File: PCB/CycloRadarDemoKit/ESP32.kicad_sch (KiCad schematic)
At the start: 18 parts, among them SW101 RESET, SW102 BOOT MODE, U101 ESP32-WROVER-E-N16R8

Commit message: PCB, 3Dmodel
mockup PCB version done, schcematic exported to latex, 3D model generated and exported to latex
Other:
- title: Safety Ride Radar Sensor -> Radar Safety Sensor
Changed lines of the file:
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@@
   (paper "A4")
   (title_block
-    (title "Safety Ride Radar Sensor")
-    (date "2023-12-19")
-    (rev "Rev.: WIP")
+    (title "Radar Safety Sensor")
+    (date "2023-12-20")
+    (rev "Rev.: 1")
     (company "ALPS Electric Czech, s.r.o.")
     (comment 1 "Designed by Martin Tavoda")

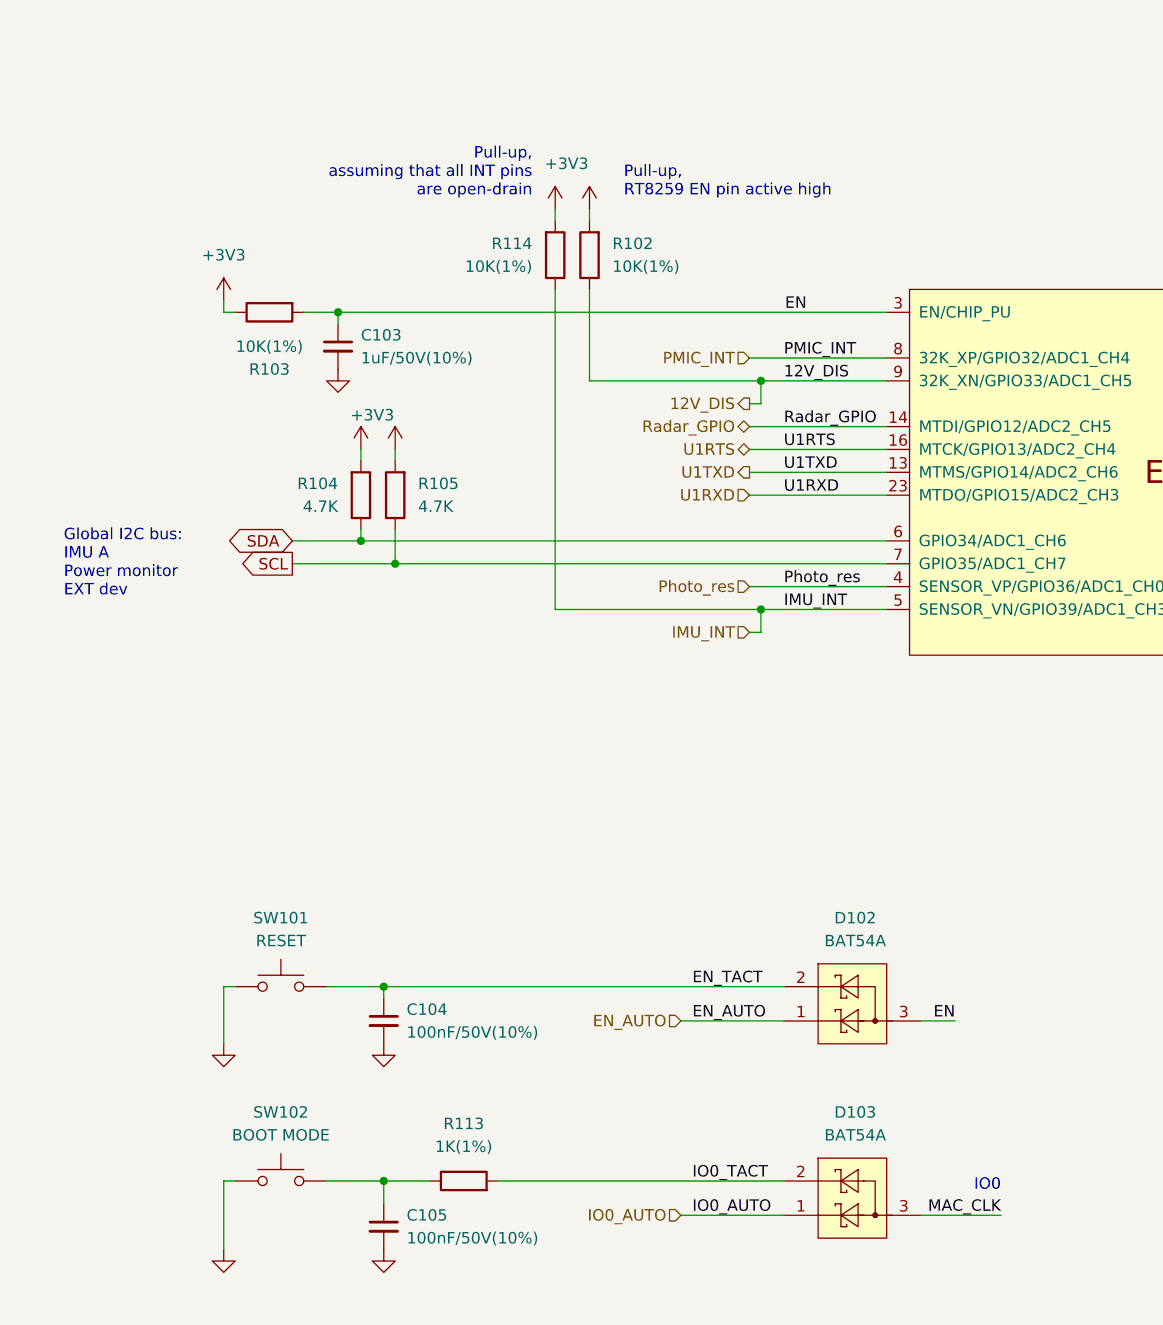
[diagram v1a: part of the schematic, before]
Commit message: sortingAbbr, cosmetics schematic, export schematic to thesis
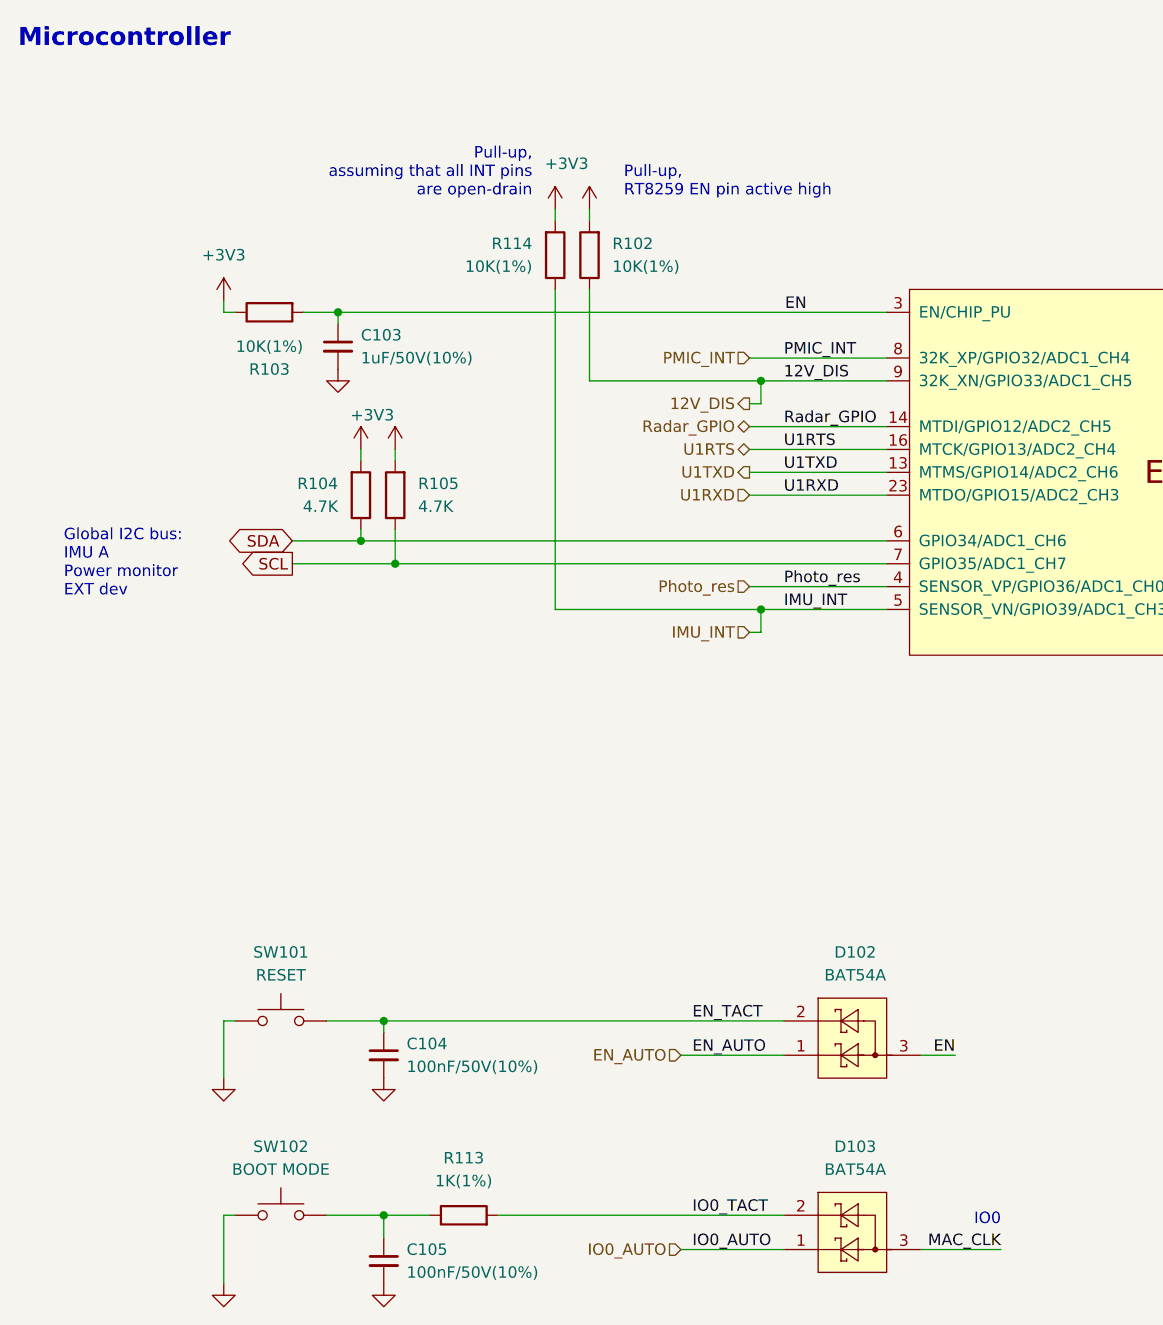
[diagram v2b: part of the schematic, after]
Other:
- note added: "Microcontroller"
- moved on the sheet: C104, C105, D102, D103, R113, SW101, SW102

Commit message: PCB small updates, schemtatic cosmetics, SEP FINAL
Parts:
- C101: footprint (none) -> Capacitor_SMD:C_0603_1608Metric; LCSC (none) -> C19702
- C102: LCSC (none) -> C19702
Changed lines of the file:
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@@
       (effects (font (size 1.27 1.27)) (justify left))
     )
-    (property "Footprint" "" (at 189.23 44.45 0)
+    (property "Footprint" "Capacitor_SMD:C_0603_1608Metric" (at 189.23 44.45 0)
       (effects (font (size 1.27 1.27)) hide)
     )
     (property "Datasheet" "~" (at 189.23 44.45 0)
+      (effects (font (size 1.27 1.27)) hide)
+    )
+    (property "LCSC" "C19702" (at 189.23 44.45 0)
       (effects (font (size 1.27 1.27)) hide)
     )
@@
       (effects (font (size 1.27 1.27)) hide)
     )
-    (property "LCSC" "" (at 184.15 44.45 0)
+    (property "LCSC" "C19702" (at 184.15 44.45 0)
       (effects (font (size 1.27 1.27)) hide)
     )

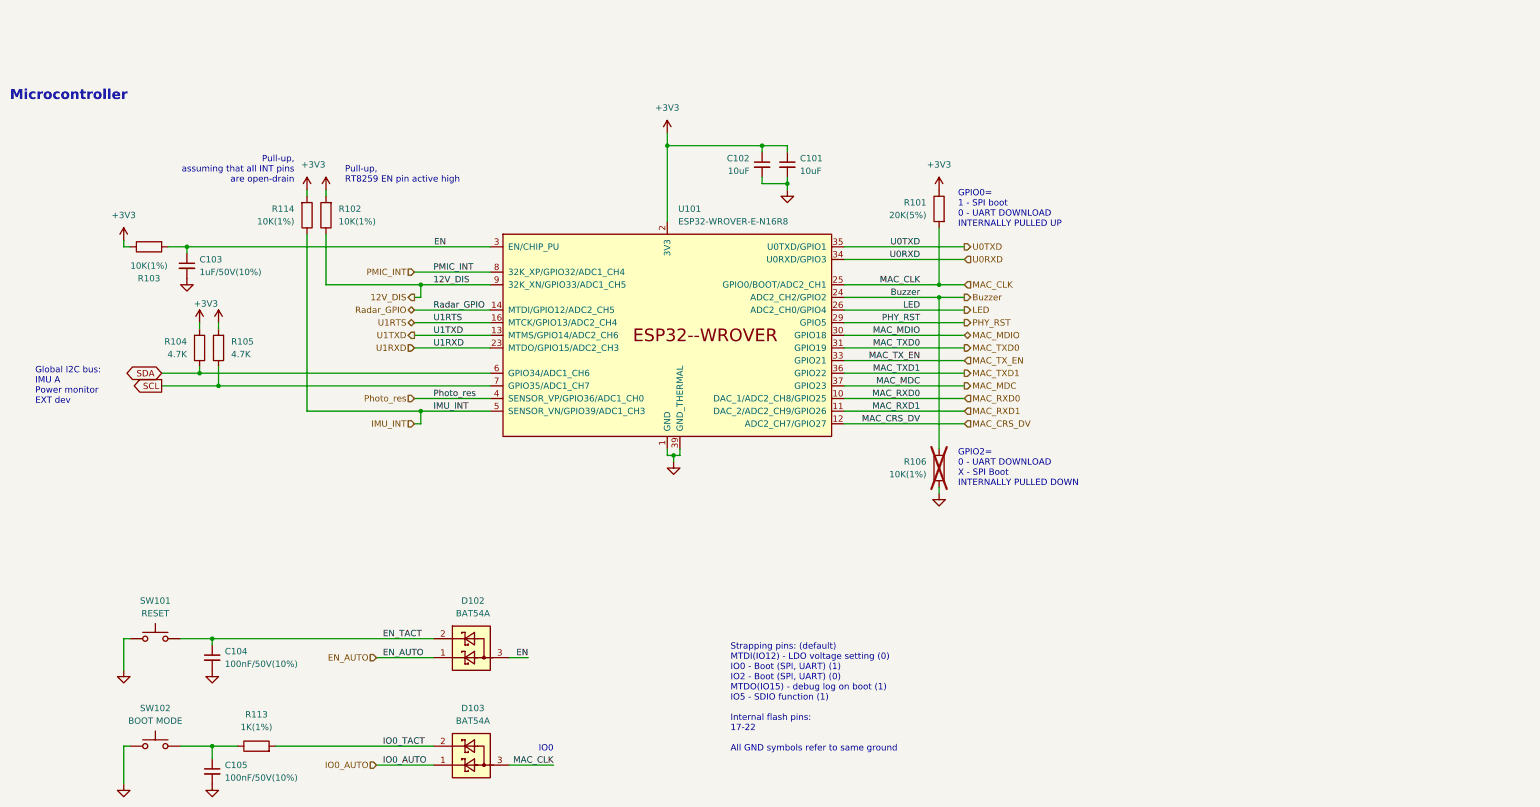
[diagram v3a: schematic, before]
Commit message: All peripherals checked, changed ESP32 pinout
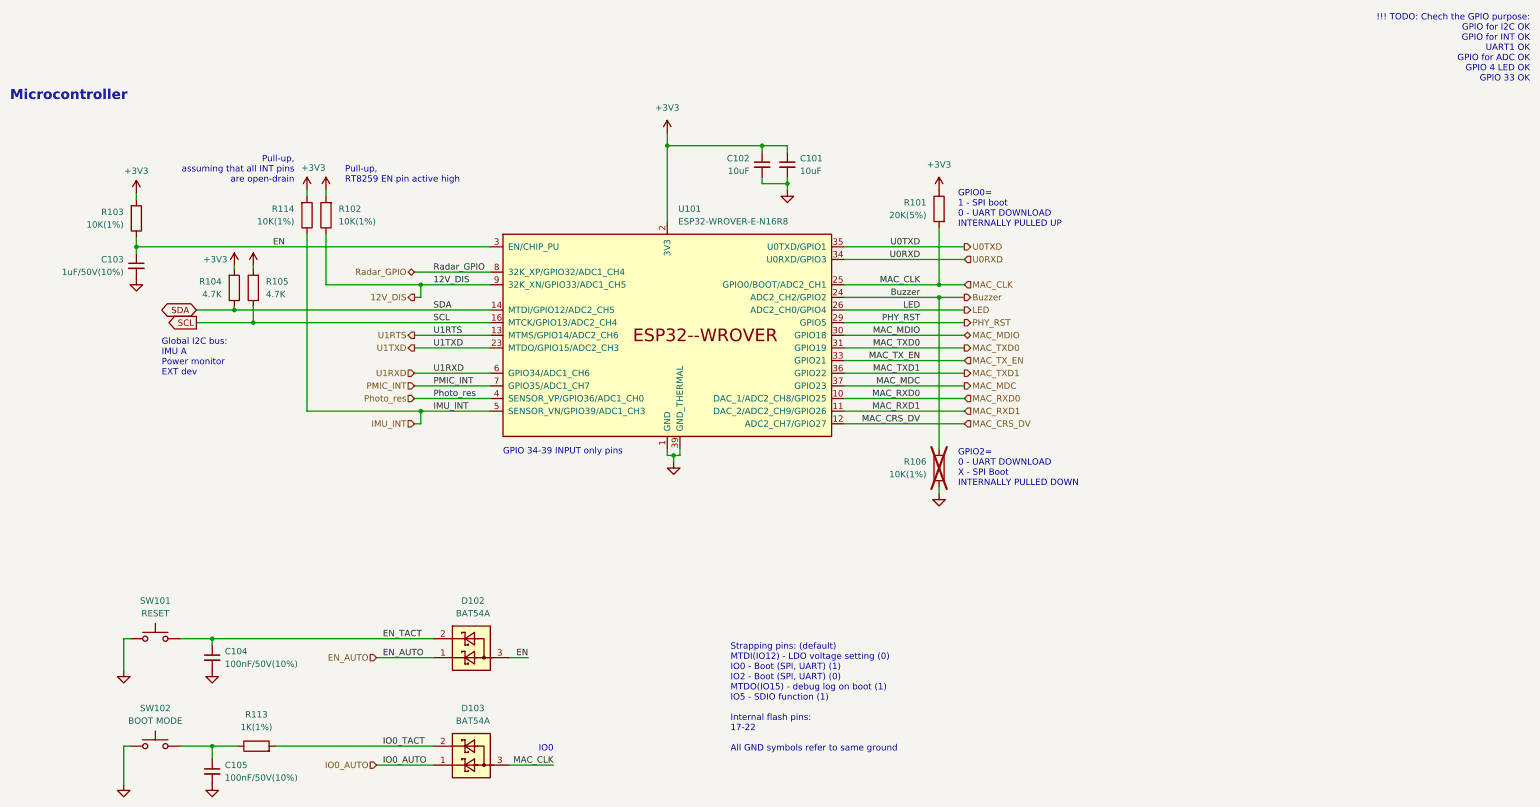
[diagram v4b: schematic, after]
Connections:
- net +3V3: now also R103.2; no longer R103.1
- net EN: now also R103.1; no longer R103.2
- net PMIC_INT: now also U101.7 (GPIO35/ADC1_CH7); no longer U101.8 (32K_XP/GPIO32/ADC1_CH4)
- net Radar_GPIO: now also U101.8 (32K_XP/GPIO32/ADC1_CH4); no longer U101.14 (MTDI/GPIO12/ADC2_CH5)
- net SCL: now also U101.16 (MTCK/GPIO13/ADC2_CH4); no longer U101.7 (GPIO35/ADC1_CH7)
- net SDA: now also U101.14 (MTDI/GPIO12/ADC2_CH5); no longer U101.6 (GPIO34/ADC1_CH6)
- net U1RTS: now also U101.13 (MTMS/GPIO14/ADC2_CH6); no longer U101.16 (MTCK/GPIO13/ADC2_CH4)
- net U1RXD: now also U101.6 (GPIO34/ADC1_CH6); no longer U101.23 (MTDO/GPIO15/ADC2_CH3)
- net U1TXD: now also U101.23 (MTDO/GPIO15/ADC2_CH3); no longer U101.13 (MTMS/GPIO14/ADC2_CH6)
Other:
- note added: "!!! TODO: Chech the GPIO purpose: GPIO for I2C OK GPIO for INT OK UART1 OK GPIO for ADC OK GPIO 4 LED OK GPIO 33 OK"
- note added: "GPIO 34-39 INPUT only pins"
- moved on the sheet: C103, R103, R104, R105

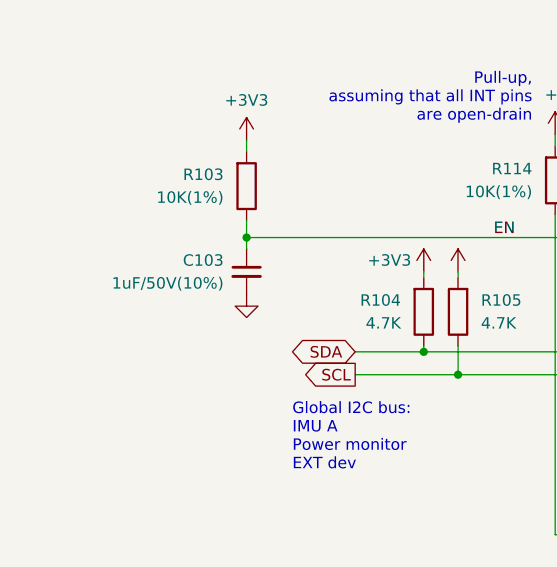
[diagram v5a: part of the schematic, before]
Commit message: Parts ordered on PCB, 1206->0803 10uF, 0803->0402 1uF
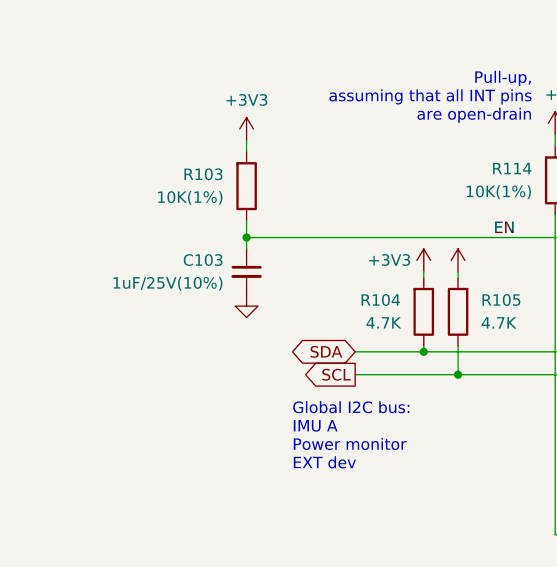
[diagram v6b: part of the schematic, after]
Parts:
- C103: value 1uF/50V(10%) -> 1uF/25V(10%); footprint Capacitor_SMD:C_0603_1608Metric -> Capacitor_SMD:C_0402_1005Metric; LCSC C15849 -> C52923
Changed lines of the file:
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@@
       (effects (font (size 1.27 1.27)) (justify left))
     )
-    (property "Value" "1uF/50V(10%)" (at 55.88 66.0463 0)
+    (property "Value" "1uF/25V(10%)" (at 55.88 66.0463 0)
       (effects (font (size 1.27 1.27)) (justify left))
     )
-    (property "Footprint" "Capacitor_SMD:C_0603_1608Metric" (at 58.42 64.77 0)
+    (property "Footprint" "Capacitor_SMD:C_0402_1005Metric" (at 58.42 64.77 0)
       (effects (font (size 1.27 1.27)) hide)
     )
@@
       (effects (font (size 1.27 1.27)) hide)
     )
-    (property "LCSC" "C15849" (at 58.42 64.77 0)
+    (property "LCSC" "C52923" (at 58.42 64.77 0)
       (effects (font (size 1.27 1.27)) hide)
     )

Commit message: RMII routed, first try
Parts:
- added R301: 0R, Resistor_SMD:R_0805_2012Metric, symbol Device:R
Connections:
- net MAC_CLK: now also R301.1; no longer D103.3
- new net: D103.3, R301.2
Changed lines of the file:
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@@
     (stroke (width 0) (type default))
   )
-  (wire (pts (xy 142.24 165.1) (xy 133.35 165.1))
+  (wire (pts (xy 142.875 165.1) (xy 153.035 165.1))
     (stroke (width 0) (type default))
   )
@@
   )
   (wire (pts (xy 165.1 40.64) (xy 165.1 55.88))
+    (stroke (width 0) (type default))
+  )
+  (wire (pts (xy 133.35 165.1) (xy 135.255 165.1))
     (stroke (width 0) (type default))
   )
@@
     (effects (font (size 1.27 1.27)) (justify left bottom))
   )
-  (text "IO0" (at 142.24 162.56 0)
+  (text "IO0" (at 153.035 162.56 0)
     (effects (font (size 1.27 1.27) (color 0 0 0 1)) (justify right bottom))
   )
@@
     (effects (font (size 1.27 1.27)) (justify left bottom))
   )
-  (label "MAC_CLK" (at 142.24 165.1 180) (fields_autoplaced)
+  (label "MAC_CLK" (at 153.035 165.1 180) (fields_autoplaced)
     (effects (font (size 1.27 1.27)) (justify right bottom))
   )
@@
         )
       )
+    )
+  )
+  (symbol (lib_id "Device:R") (at 139.065 165.1 270) (unit 1)
+    (in_bom yes) (on_board yes) (dnp no) (fields_autoplaced)
+    (property "Reference" "R301" (at 139.065 158.75 90)
+      (effects (font (size 1.27 1.27)))
+    )
+    (property "Value" "0R" (at 139.065 161.29 90)
+      (effects (font (size 1.27 1.27)))
+    )
+    (property "Footprint" "Resistor_SMD:R_0805_2012Metric" (at 139.065 163.322 90)
+      (effects (font (size 1.27 1.27)) hide)
+    )
+    (property "Datasheet" "~" (at 139.065 165.1 0)
+      (effects (font (size 1.27 1.27)) hide)
+    )
+    (property "LCSC" "C17477" (at 139.065 165.1 0)
+      (effects (font (size 1.27 1.27)) hide)
+    )
+    (pin "1")
+    (pin "2")
+    (instances
+      (project "CycloRadarDemoKit"
+        (path "/c2cd7ca4-4652-4b3d-a3a8-1cfa66cb11e9/8ae18a6c-482d-4e1c-94d1-12de0ef4fa68"
+          (reference "R301") (unit 1)
+        )
+        (path "/c2cd7ca4-4652-4b3d-a3a8-1cfa66cb11e9/8e86b850-15ce-40c4-bda7-5d0afa1e377d"
+          (reference "R418") (unit 1)
+        )
+        (path "/c2cd7ca4-4652-4b3d-a3a8-1cfa66cb11e9/621cac9b-ef3d-4a37-be45-aae7901810ec"
+          (reference "R505") (unit 1)
+        )
+      )

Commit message: start of repair after review
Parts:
- R101: value 20K(5%) -> 20K(1%)
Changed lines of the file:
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@@
       (effects (font (size 1.27 1.27)) (justify left))
     )
-    (property "Value" "20K(5%)" (at 217.17 54.61 0)
+    (property "Value" "20K(1%)" (at 217.17 54.61 0)
       (effects (font (size 1.27 1.27)) (justify left))
     )
